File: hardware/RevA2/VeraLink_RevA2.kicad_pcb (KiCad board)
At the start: 4 copper layers, 42 x 42 mm, 55 parts, among them J1 MAG_POGO_3PIN, J2 FACTORY_SWD_PADS, M1 COIN_LRA_MOTOR, SW1 USER_BUTTON, U1 MCP73831-2-OT, U2 TPS78233DDC, U3 nRF52840-QIAA, U4 E22-900M22S_SX1262_LORA, U5 DRV2605LDGS, Y1 32MHz, Y2 32.768 kHZ

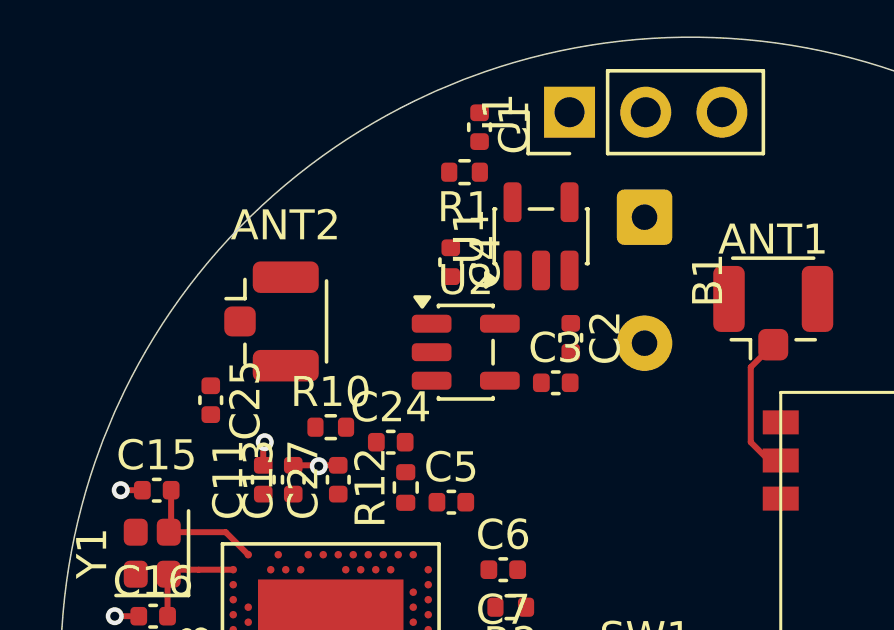
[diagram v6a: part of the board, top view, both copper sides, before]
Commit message: Route Rev A2 regulator SYS_3V3 output section
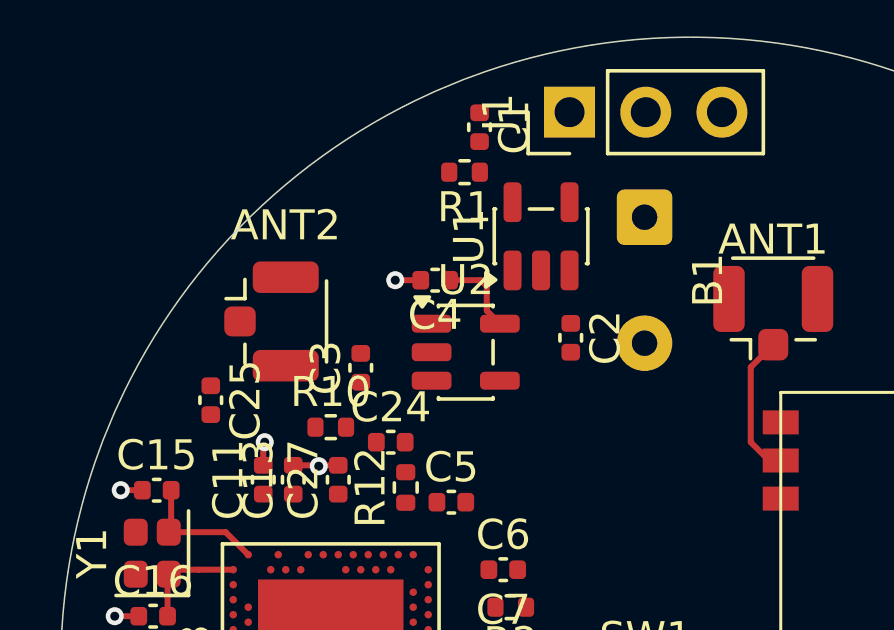
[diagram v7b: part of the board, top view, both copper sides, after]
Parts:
- moved C3 6.52 mm to (133.0, 97.5), turned to 90 degrees
- moved C4 0.79 mm to (135.5, 94.6), turned to 180 degrees
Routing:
- net /SYS_3V3: track 0.00 -> 2.75 mm
- net GND: track 7.46 -> 8.52 mm, vias 6 -> 7
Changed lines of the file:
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@@
 	(footprint "Capacitor_SMD:C_0402_1005Metric"
 		(layer "F.Cu")
-		(at 136 94 -90)
+		(at 135.48 94.6 180)
 		(descr "Capacitor SMD 0402 (1005 Metric), square (rectangular) end terminal, IPC-7351 nominal, (Body size source: IPC-SM-782 page 76, https://www.pcb-3d.com/wordpress/wp-content/uploads/ipc-sm-782a_amendment_1_and_2.pdf)")
 		(tags "capacitor")
 		(property "Reference" "C4"
-			(at 0 -1.16 270)
+			(at 0 -1.16 0)
 			(layer "F.SilkS")
 			(effects
@@
 		)
 		(property "Value" "4.7uF"
-			(at 0 1.16 270)
+			(at 0 1.16 0)
 			(layer "F.Fab")
 			(effects
@@
 		)
 		(property "Datasheet" ""
-			(at 0 0 270)
+			(at 0 0 0)
 			(layer "F.Fab")
 			(hide yes)
@@
 		)
 		(property "Description" "Unpolarized capacitor"
-			(at 0 0 270)
+			(at 0 0 0)
 			(layer "F.Fab")
 			(hide yes)
@@
 		)
 		(property "KiLib_Generator" "SMD_2terminal_chip_molded"
-			(at 0 0 270)
+			(at 0 0 0)
 			(layer "F.SilkS")
 			(hide yes)
@@
 		)
 		(fp_text user "${REFERENCE}"
-			(at 0 0 270)
+			(at 0 0 0)
 			(layer "F.Fab")
 			(effects
@@
 		)
 		(pad "1" smd roundrect
-			(at -0.48 0 270)
+			(at -0.48 0 180)
 			(size 0.56 0.62)
 			(layers "F.Cu" "F.Mask" "F.Paste")
@@
 		)
 		(pad "2" smd roundrect
-			(at 0.48 0 270)
+			(at 0.48 0 180)
 			(size 0.56 0.62)
 			(layers "F.Cu" "F.Mask" "F.Paste")
@@
 	(footprint "Capacitor_SMD:C_0402_1005Metric"
 		(layer "F.Cu")
-		(at 139.5 98.02)
+		(at 133 97.52 90)
 		(descr "Capacitor SMD 0402 (1005 Metric), square (rectangular) end terminal, IPC-7351 nominal, (Body size source: IPC-SM-782 page 76, https://www.pcb-3d.com/wordpress/wp-content/uploads/ipc-sm-782a_amendment_1_and_2.pdf)")
 		(tags "capacitor")
 		(property "Reference" "C3"
-			(at 0 -1.16 0)
+			(at 0 -1.16 90)
 			(layer "F.SilkS")
 			(effects
@@
 		)
 		(property "Value" "4.7uF"
-			(at 0 1.16 0)
+			(at 0 1.16 90)
 			(layer "F.Fab")
 			(effects
@@
 		)
 		(property "Datasheet" ""
-			(at 0 0 0)
+			(at 0 0 90)
 			(layer "F.Fab")
 			(hide yes)
@@
 		)
 		(property "Description" "Unpolarized capacitor"
-			(at 0 0 0)
+			(at 0 0 90)
 			(layer "F.Fab")
 			(hide yes)
@@
 		)
 		(property "KiLib_Generator" "SMD_2terminal_chip_molded"
-			(at 0 0 0)
+			(at 0 0 90)
 			(layer "F.SilkS")
 			(hide yes)
@@
 		)
 		(fp_text user "${REFERENCE}"
-			(at 0 0 0)
+			(at 0 0 90)
 			(layer "F.Fab")
 			(effects
@@
 		)
 		(pad "1" smd roundrect
-			(at -0.48 0)
+			(at -0.48 0 90)
 			(size 0.56 0.62)
 			(layers "F.Cu" "F.Mask" "F.Paste")
@@
 		)
 		(pad "2" smd roundrect
-			(at 0.48 0)
+			(at 0.48 0 90)
 			(size 0.56 0.62)
 			(layers "F.Cu" "F.Mask" "F.Paste")
@@
 	)
 	(segment
+		(start 135 94.6)
+		(end 134.15 94.6)
+		(width 0.2)
+		(layer "F.Cu")
+		(net "GND")
+	)
+	(segment
 		(start 129.75 100.05)
 		(end 129.8 100)
@@
 	)
 	(segment
+		(start 134 94.75)
+		(end 134.15 94.6)
+		(width 0.2)
+		(layer "F.Cu")
+		(net "GND")
+	)
+	(segment
 		(start 128.5 116.5)
 		(end 128.5 116.7)
@@
 	)
 	(via
+		(at 134.15 94.6)
+		(size 0.6)
+		(drill 0.3)
+		(layers "F.Cu" "B.Cu")
+		(net "GND")
+	)
+	(via
 		(at 124.8 105.8)
 		(size 0.6)
@@
 	)
 	(segment
+		(start 137 94.6)
+		(end 137.2 94.8)
+		(width 0.2)
+		(layer "F.Cu")
+		(net "/SYS_3V3")
+	)
+	(segment
+		(start 135.96 94.6)
+		(end 137 94.6)
+		(width 0.2)
+		(layer "F.Cu")
+		(net "/SYS_3V3")
+	)
+	(segment
+		(start 137.2 94.8)
+		(end 137.2 95.6125)
+		(width 0.2)
+		(layer "F.Cu")
+		(net "/SYS_3V3")
+	)
+	(segment
+		(start 137.2 95.6125)
+		(end 137.6375 96.05)
+		(width 0.2)
+		(layer "F.Cu")
+		(net "/SYS_3V3")
+	)
+	(segment

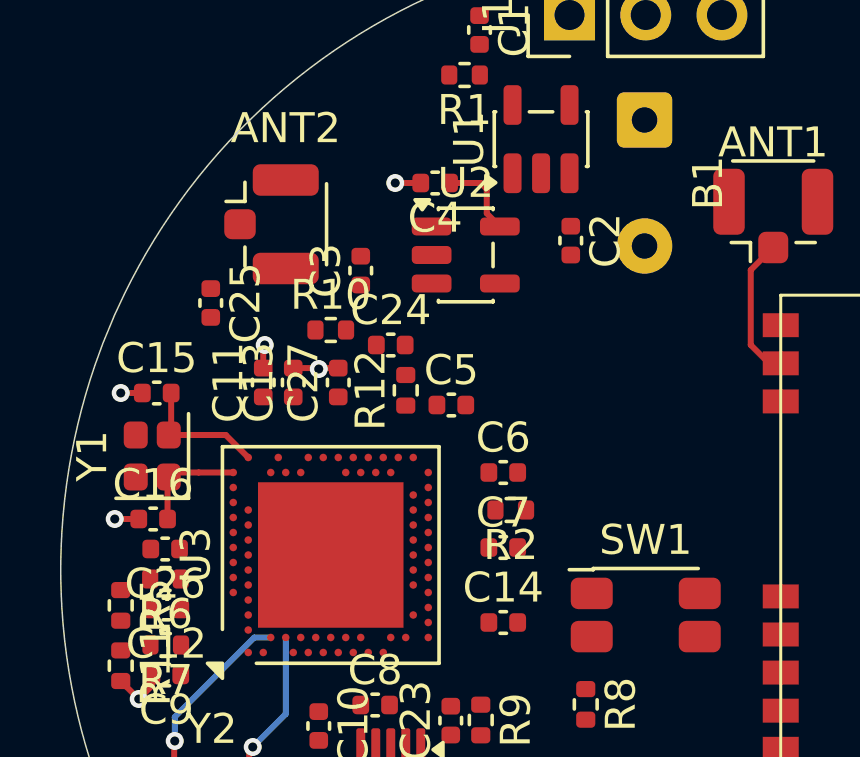
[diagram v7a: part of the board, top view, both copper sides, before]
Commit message: Route Rev A2 SYS_3V3 main feed to U3 area
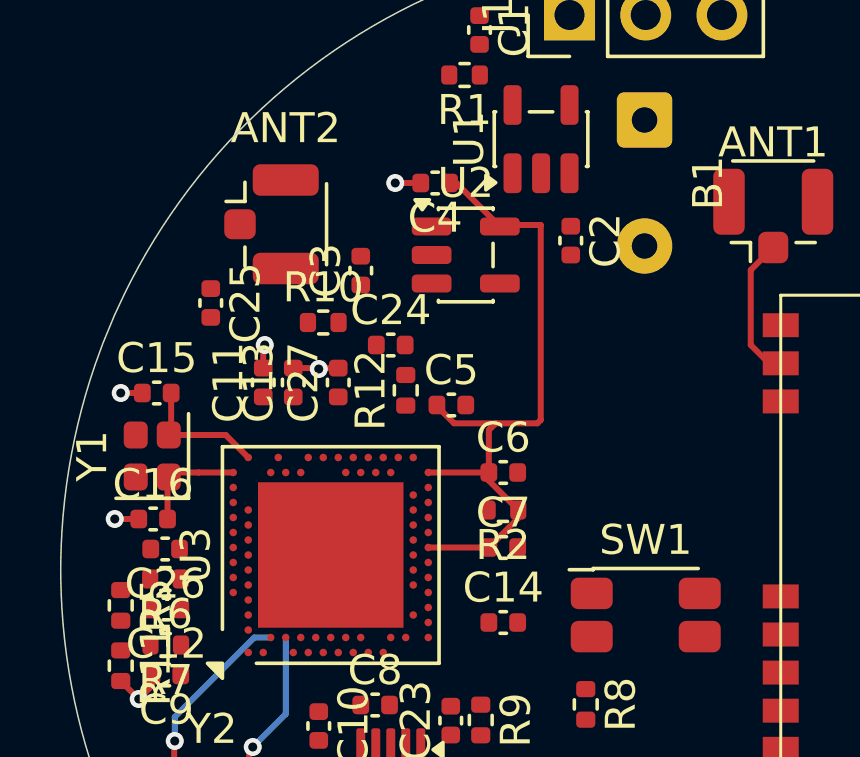
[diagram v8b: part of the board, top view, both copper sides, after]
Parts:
- moved R10 0.35 mm to (131.8, 99.2)
- moved R2 0.26 mm to (137.7, 105.5)
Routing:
- net /SYS_3V3: track 2.75 -> 23.0 mm
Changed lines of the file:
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@@
 	(footprint "Resistor_SMD:R_0402_1005Metric"
 		(layer "F.Cu")
-		(at 132 99.5)
+		(at 131.75 99.25)
 		(descr "Resistor SMD 0402 (1005 Metric), square (rectangular) end terminal, IPC-7351 nominal, (Body size source: IPC-SM-782 page 72, https://www.pcb-3d.com/wordpress/wp-content/uploads/ipc-sm-782a_amendment_1_and_2.pdf)")
 		(tags "resistor")
@@
 	(footprint "Resistor_SMD:R_0402_1005Metric"
 		(layer "F.Cu")
-		(at 138 105.5 180)
+		(at 137.74 105.5 180)
 		(descr "Resistor SMD 0402 (1005 Metric), square (rectangular) end terminal, IPC-7351 nominal, (Body size source: IPC-SM-782 page 72, https://www.pcb-3d.com/wordpress/wp-content/uploads/ipc-sm-782a_amendment_1_and_2.pdf)")
 		(tags "resistor")
@@
 	)
 	(segment
-		(start 137 94.6)
-		(end 137.2 94.8)
+		(start 137.6375 96.05)
+		(end 136.1875 94.6)
 		(width 0.2)
 		(layer "F.Cu")
@@
 	)
 	(segment
-		(start 135.96 94.6)
-		(end 137 94.6)
+		(start 137.5 102.61)
+		(end 138.89 102.61)
 		(width 0.2)
 		(layer "F.Cu")
@@
 	)
 	(segment
-		(start 137.2 94.8)
-		(end 137.2 95.6125)
+		(start 137.27 104.25)
+		(end 137.27 104.52)
 		(width 0.2)
 		(layer "F.Cu")
@@
 	)
 	(segment
-		(start 137.2 95.6125)
-		(end 137.6375 96.05)
+		(start 138.25 105.5)
+		(end 138.25 105.77)
+		(width 0.2)
+		(layer "F.Cu")
+		(net "/SYS_3V3")
+	)
+	(segment
+		(start 137.27 104.52)
+		(end 138.25 105.5)
+		(width 0.2)
+		(layer "F.Cu")
+		(net "/SYS_3V3")
+	)
+	(segment
+		(start 137.27 104.25)
+		(end 137.27 102.84)
+		(width 0.2)
+		(layer "F.Cu")
+		(net "/SYS_3V3")
+	)
+	(segment
+		(start 135.54 102)
+		(end 135.54 102.04)
+		(width 0.2)
+		(layer "F.Cu")
+		(net "/SYS_3V3")
+	)
+	(segment
+		(start 137.27 106.75)
+		(end 135.25 106.75)
+		(width 0.2)
+		(layer "F.Cu")
+		(net "/SYS_3V3")
+	)
+	(segment
+		(start 138.25 105.77)
+		(end 137.27 106.75)
+		(width 0.2)
+		(layer "F.Cu")
+		(net "/SYS_3V3")
+	)
+	(segment
+		(start 137.27 104.25)
+		(end 135.25 104.25)
+		(width 0.2)
+		(layer "F.Cu")
+		(net "/SYS_3V3")
+	)
+	(segment
+		(start 136.11 102.61)
+		(end 137.5 102.61)
+		(width 0.2)
+		(layer "F.Cu")
+		(net "/SYS_3V3")
+	)
+	(segment
+		(start 137.6375 96.05)
+		(end 137.6875 96)
+		(width 0.2)
+		(layer "F.Cu")
+		(net "/SYS_3V3")
+	)
+	(segment
+		(start 135.54 102.04)
+		(end 136.11 102.61)
+		(width 0.2)
+		(layer "F.Cu")
+		(net "/SYS_3V3")
+	)
+	(segment
+		(start 137.6875 96)
+		(end 139 96)
+		(width 0.2)
+		(layer "F.Cu")
+		(net "/SYS_3V3")
+	)
+	(segment
+		(start 139 96)
+		(end 139 102.5)
+		(width 0.2)
+		(layer "F.Cu")
+		(net "/SYS_3V3")
+	)
+	(segment
+		(start 138.89 102.61)
+		(end 139 102.5)
+		(width 0.2)
+		(layer "F.Cu")
+		(net "/SYS_3V3")
+	)
+	(segment
+		(start 137.27 102.84)
+		(end 137.5 102.61)
+		(width 0.2)
+		(layer "F.Cu")
+		(net "/SYS_3V3")
+	)
+	(segment
+		(start 136.1875 94.6)
+		(end 135.96 94.6)
 		(width 0.2)
 		(layer "F.Cu")
